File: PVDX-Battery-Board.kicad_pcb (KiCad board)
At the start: 2 copper layers, 75.7 x 115 mm, 44 parts, among them J1 Conn_01x19, J10 Conn_01x02_Pin, J11 Conn_01x02_Pin, J12 Conn_01x02, J2 Conn_01x06, J3 Conn_01x10, J4 Conn_01x02_Pin, J5 Conn_01x02_Pin, J6 Conn_01x02_Pin, J7 Conn_01x02_Pin, J8 Conn_01x02_Pin, J9 Conn_01x02_Pin, Q1 DMC2053UVT, Q2 DMC2053UVT

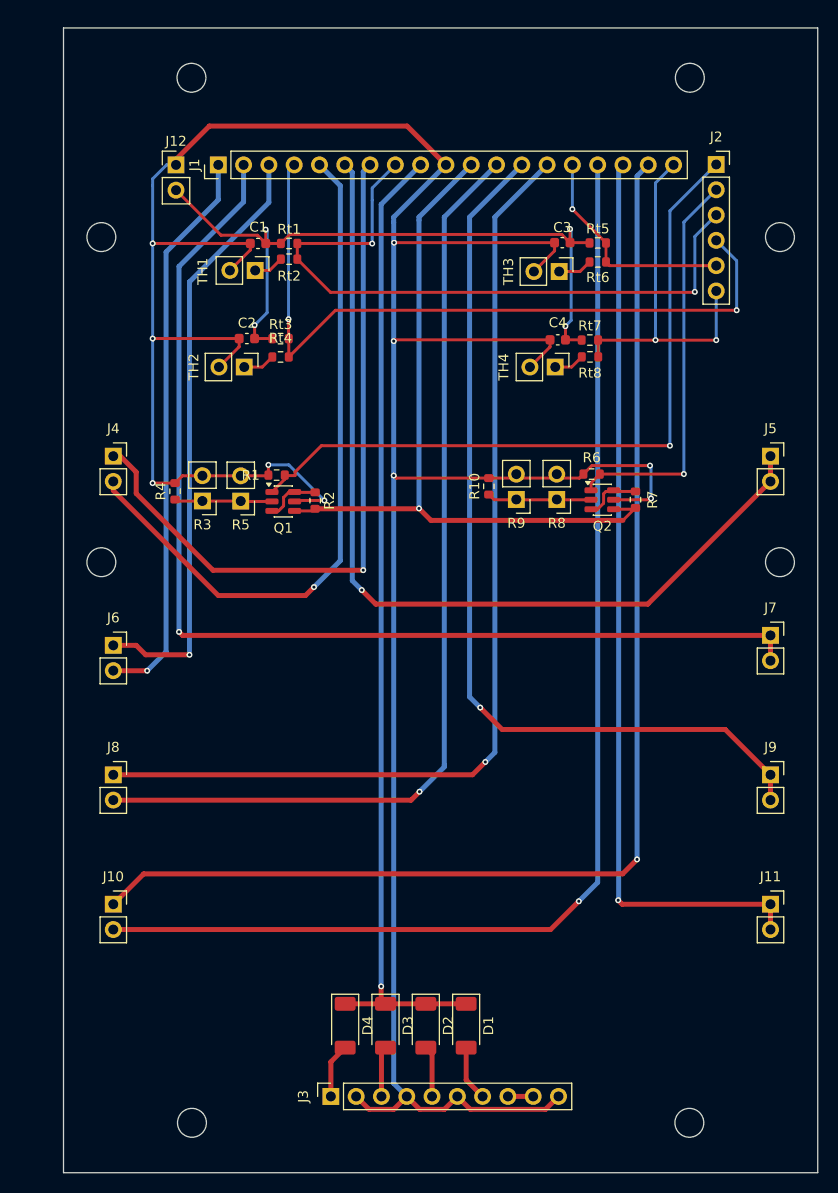
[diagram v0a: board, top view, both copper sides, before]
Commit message: Add battery overdischarge & short protections to board
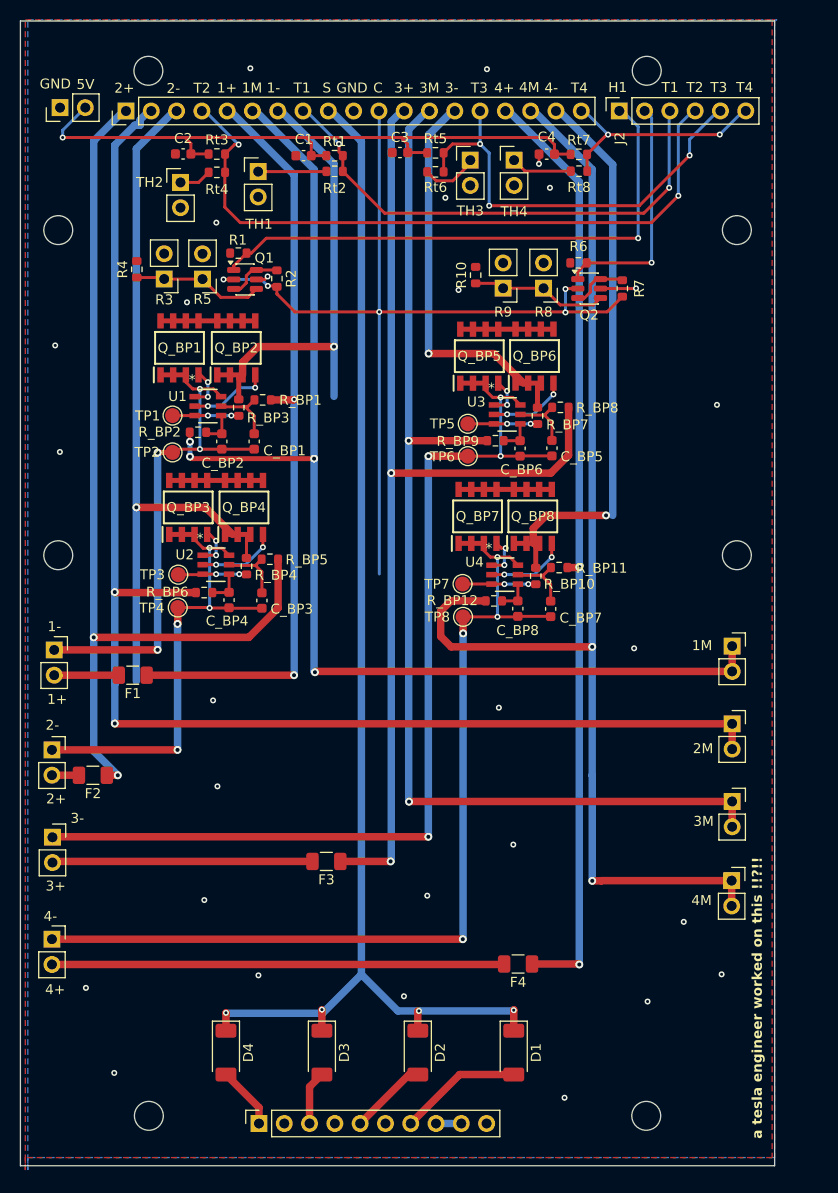
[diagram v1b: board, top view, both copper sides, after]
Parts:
- added C_BP1: 0.1u, Capacitor_SMD:C_0603_1608Metric, F.Cu at (124.2, 76.5)
- added C_BP2: 0.1u, Capacitor_SMD:C_0603_1608Metric, F.Cu at (120.9, 76.5)
- added C_BP3: 0.1u, Capacitor_SMD:C_0603_1608Metric, F.Cu at (124.9, 92.5)
- added C_BP4: 0.1u, Capacitor_SMD:C_0603_1608Metric, F.Cu at (121.6, 92.5)
- added C_BP5: 0.1u, Capacitor_SMD:C_0603_1608Metric, F.Cu at (154.1, 77.2)
- added C_BP6: 0.1u, Capacitor_SMD:C_0603_1608Metric, F.Cu at (150.8, 77.2)
- added C_BP7: 0.1u, Capacitor_SMD:C_0603_1608Metric, F.Cu at (153.9, 93.3)
- added C_BP8: 0.1u, Capacitor_SMD:C_0603_1608Metric, F.Cu at (150.6, 93.3)
- added F1: 3410.0141.01, Fuse:Fuse_1206_3216Metric, F.Cu at (112.0, 100.0)
- added F2: 3410.0141.01, Fuse:Fuse_1206_3216Metric, F.Cu at (108.0, 110.0)
- added F3: 3410.0141.01, Fuse:Fuse_1206_3216Metric, F.Cu at (131.4, 118.7)
- added F4: 3410.0141.01, Fuse:Fuse_1206_3216Metric, F.Cu at (150.7, 129.0)
- added Q_BP1: SI4136DY-T1-GE3, footprints:SOIC127P600X175-8N, F.Cu at (116.7, 67.1)
- added Q_BP2: SI4136DY-T1-GE3, footprints:SOIC127P600X175-8N, F.Cu at (122.3, 67.1)
- added Q_BP3: SI4136DY-T1-GE3, footprints:SOIC127P600X175-8N, F.Cu at (117.5, 83.2)
- added Q_BP4: SI4136DY-T1-GE3, footprints:SOIC127P600X175-8N, F.Cu at (123.1, 83.2)
- added Q_BP5: SI4136DY-T1-GE3, footprints:SOIC127P600X175-8N, F.Cu at (146.8, 68.0)
- added Q_BP6: SI4136DY-T1-GE3, footprints:SOIC127P600X175-8N, F.Cu at (152.3, 68.0)
- added Q_BP7: SI4136DY-T1-GE3, footprints:SOIC127P600X175-8N, F.Cu at (146.6, 84.0)
- added Q_BP8: SI4136DY-T1-GE3, footprints:SOIC127P600X175-8N, F.Cu at (152.1, 84.0)
- added R_BP1: 470R, Resistor_SMD:R_0603_1608Metric, F.Cu at (125.0, 72.3)
- added R_BP10: 2k, Resistor_SMD:R_0603_1608Metric, F.Cu at (152.4, 90.0)
- added R_BP11: 470R, Resistor_SMD:R_0603_1608Metric, F.Cu at (154.8, 89.2)
- added R_BP12: 470R, Resistor_SMD:R_0603_1608Metric, F.Cu at (148.2, 92.5)
- added R_BP2: 470R, Resistor_SMD:R_0603_1608Metric, F.Cu at (118.5, 75.6)
- added R_BP3: 2k, Resistor_SMD:R_0603_1608Metric, F.Cu at (122.6, 73.1)
- added R_BP4: 2k, Resistor_SMD:R_0603_1608Metric, F.Cu at (123.4, 89.0)
- added R_BP5: 470R, Resistor_SMD:R_0603_1608Metric, F.Cu at (125.7, 88.3)
- added R_BP6: 470R, Resistor_SMD:R_0603_1608Metric, F.Cu at (119.1, 91.7)
- added R_BP7: 2k, Resistor_SMD:R_0603_1608Metric, F.Cu at (152.6, 74.0)
- added R_BP8: 470R, Resistor_SMD:R_0603_1608Metric, F.Cu at (154.9, 73.1)
- added R_BP9: 470R, Resistor_SMD:R_0603_1608Metric, F.Cu at (148.4, 76.5)
- added TP1: TestPoint, TestPoint:TestPoint_Pad_D1.5mm, F.Cu at (116.0, 73.9)
- added TP2: TestPoint, TestPoint:TestPoint_Pad_D1.5mm, F.Cu at (116.0, 77.6)
- added TP3: TestPoint, TestPoint:TestPoint_Pad_D1.5mm, F.Cu at (116.5, 89.9)
- added TP4: TestPoint, TestPoint:TestPoint_Pad_D1.5mm, F.Cu at (116.5, 93.2)
- added TP5: TestPoint, TestPoint:TestPoint_Pad_D1.5mm, F.Cu at (145.6, 74.8)
- added TP6: TestPoint, TestPoint:TestPoint_Pad_D1.5mm, F.Cu at (145.6, 78.0)
- added TP7: TestPoint, TestPoint:TestPoint_Pad_D1.5mm, F.Cu at (145.1, 90.8)
- added TP8: TestPoint, TestPoint:TestPoint_Pad_D1.5mm, F.Cu at (145.1, 94.1)
- added U1: S-8252ABY-M6T1U, footprints:SOT236-A-PKG_MP006-A-P-SD-2.1_ABY, F.Cu at (119.5, 73.0)
- added U2: S-8252ABY-M6T1U, footprints:SOT236-A-PKG_MP006-A-P-SD-2.1_ABY, F.Cu at (120.3, 88.9)
- added U3: S-8252ABY-M6T1U, footprints:SOT236-A-PKG_MP006-A-P-SD-2.1_ABY, F.Cu at (149.6, 73.8)
- added U4: S-8252ABY-M6T1U, footprints:SOT236-A-PKG_MP006-A-P-SD-2.1_ABY, F.Cu at (149.3, 89.9)
- C1, C2, C3, C4: value .1u -> 0.1u
- Rt1, Rt3, Rt5, Rt7: value 15.8k -> 42k
- Rt2, Rt4, Rt6, Rt8: value 5.83k -> 12k
- moved R1 22.6 mm to (122.6, 57.6)
- moved R2 22.6 mm to (126.4, 60.2)
- moved R3 22.6 mm to (115.1, 60.2)
- moved R4 22.6 mm to (112.4, 59.2)
- moved R5 22.6 mm to (119.0, 60.2)
- moved Q1 22.6 mm to (123.2, 60.3)
- moved R7 21.3 mm to (161.1, 61.2)
- moved R10 21.3 mm to (146.4, 59.8)
- moved Q2 21.3 mm to (157.8, 61.2)
- moved R6 21.3 mm to (156.7, 58.6)
- moved R8 21.3 mm to (153.2, 61.1)
- moved R9 21.3 mm to (149.2, 61.1)
- moved TH4 21.2 mm to (150.2, 48.3), turned to 0 degrees
- moved J4 20.3 mm to (104.1, 97.5)
- moved C2 19.6 mm to (117.0, 47.6)
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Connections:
- J1 pad 14: BATT3- -> BATT3-P
- J1 pad 18: BATT4- -> BATT4-P
- J1 pad 3: BATT2- -> BATT2-P
- J1 pad 7: BATT1- -> BATT1-P
- J10 pad 2: BATT4+ -> Net-(BT8-+)
- J4 pad 2: BATT1+ -> Net-(BT2-+)
- J6 pad 2: BATT2+ -> Net-(BT4-+)
- J8 pad 2: BATT3+ -> Net-(BT6-+)
- Q1 pad 2: Net-(Q1B-S) -> CHG_OUT
- Q1 pad 4: CHG_OUT -> Net-(Q1B-D)
- Q2 pad 2: Net-(Q2B-S) -> CHG_OUT
- Q2 pad 4: CHG_OUT -> Net-(Q2B-D)
- R10 pad 1: Net-(Q2B-S) -> Net-(Q2B-D)
- R3 pad 1: Net-(Q1B-S) -> Net-(Q1B-D)
- R4 pad 1: Net-(Q1B-S) -> Net-(Q1B-D)
- R5 pad 1: Net-(Q1B-S) -> Net-(Q1B-D)
- R8 pad 1: Net-(Q2B-S) -> Net-(Q2B-D)
- R9 pad 1: Net-(Q2B-S) -> Net-(Q2B-D)
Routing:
- net SOLAR_1s_GND: track 306.3 -> 5.82 mm, vias 10 -> 28
- net BATT2-P: track 0.00 -> 75.1 mm, vias 0 -> 1
- net BATT4-P: track 0.00 -> 57.7 mm, vias 0 -> 1
- net BATT1-P: track 0.00 -> 47.5 mm, vias 0 -> 1
- net Net-(BT8-+): track 0.00 -> 45.4 mm
- net BATT3-P: track 0.00 -> 41.7 mm, vias 0 -> 1
- net BATT2+: track 57.2 -> 95.1 mm, vias 1 -> 2
- net SOLAR: track 98.2 -> 128.4 mm, vias 1 -> 4
- net BATT4-: track 124.7 -> 96.0 mm, vias 1 -> 4
- net BATT4M: track 92.1 -> 119.8 mm, vias 1 -> 2
- net BATT4+: track 122.7 -> 95.0 mm, vias 1 -> 2
- net Net-(BT6-+): track 0.00 -> 26.2 mm
- net BATT1M: track 92.7 -> 118.5 mm, vias 1 -> 4
- net BATT2M: track 111.7 -> 136.4 mm, vias 1 -> 2
- net BATT3M: track 91.6 -> 113.4 mm, vias 1 -> 2
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- added copper zone on B.Cu, net SOLAR_1s_GND
- added copper zone on F.Cu, net SOLAR_1s_GND
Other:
- board text added: "1+"
- board text added: "1-"
- board text added: "1M"
- board text added: "2+"
- board text added: "2-"
- board text added: "2M"
- board text added: "3+"
- board text added: "3-"
- board text added: "3M"
- board text added: "4+"
- board text added: "4-"
- board text added: "4M"
- board text added: "5V"
- board text added: "C"
- board text added: "GND"
- board text added: "H1"
- board text added: "S"
- board text added: "T1"
- board text added: "T2"
- board text added: "T3"
- board text added: "T4"
- board text added: "W/ BATT PROTECTION"
- board text added: "a tesla engineer worked on this !!?!!"
- board text added: "ever true :)"

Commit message: Fix minor issues
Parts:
- Rt1, Rt3, Rt5, Rt7: value 42k -> 11k
- Rt2, Rt4, Rt6, Rt8: value 12k -> 3.9k
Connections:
- net +5V renamed +3V3
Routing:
- net CHG_OUT: track 93.9 -> 67.6 mm
- net BATT1-P: track 47.5 -> 42.5 mm
- net BATT1M: track 118.5 -> 119.2 mm
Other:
- board text added: "3V3"
- board text removed: "5V"
